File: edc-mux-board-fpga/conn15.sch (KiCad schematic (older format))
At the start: 0 parts

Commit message: copied conn0 sheet to rest of connectors
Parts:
- added C? (x2): 2.2uF X7R, symbol Device:C_Small
- added C? (x6): 1uF, symbol Device:C_Small
- added C? (x8): 100nF, symbol Device:C_Small
- added C? (x2): 33pF, symbol Device:C_Small
- added C? (x2): 10uF, symbol Device:C_Small
- added FB?: 220Ω/2A, Resistor_SMD:R_0603_1608Metric, symbol Device:Ferrite_Bead_Small
- added J?: Device 15, Connector_PinHeader_2.54mm:PinHeader_1x12_P2.54mm_Vertical, symbol Connector_Generic:Conn_01x12
- added R? (x2): 750Ω, symbol Device:R_Small_US
- added U?: TLV320AIC3206, Package_DFN_QFN:UQFN-40-1EP_5x5mm_P0.4mm_EP3.8x3.8mm_ThermalVias, symbol SW-Texas:TLV320AIC3206
- added U?: MAX4910, Package_DFN_QFN:TQFN-16-1EP_3x3mm_P0.5mm_EP1.23x1.23mm, symbol SW-dallas-semi-maxim:MAX4910
- added U?: P82B96, symbol Interface_Expansion:P82B96
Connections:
- new net: C?.1, C?.2, U?.17 (IN1_L)
- new net: C?.1, C?.2, U?.18 (IN1_R)
- new net: C?.2, U?.19 (IN2_L), U?.20 (IN2_R)
- new net: C?.2, U?.22 (REF)
- new net: C?.2, U?.24 (IN3_L), U?.25 (IN3_R)
- new net: C?.2, U?.26 (LINE_OUT_L)
- new net: C?.2, U?.27 (LINE_OUT_R)
- new net: FB?.1, U?.28 (GND_SENSE), U?.3 (NO2)
- new net: U?.15 (NO1), U?.31 (HPL)
- new net: U?.33 (HPR), U?.7 (NO3)
- new net: C?.2, U?.35 (VNEG)
- new net: C?.1, U?.36 (FLY_N)
- new net: C?.2, U?.38 (FLY_P)
- new net: C?.2, J?.2 (Pin_2)
- new net: C?.2, J?.3 (Pin_3)
- new net: C?.1, U?.1 (NC1)
- new net: C?.1, U?.9 (NC3)
- new net +12V: C?.1, J?.12 (Pin_12), R?.1, R?.1, U?.8 (VCC)
- new net +1V8: C?.2, C?.2, U?.30 (VSYS), U?.40 (DVDD)
- new net +1V8A: C?.2, C?.2, C?.2, U?.29 (AVDD), U?.32 (DRVDD_HP), U?.39 (DVDD_CP)
- new net +3V3: C?.1, C?.2, C?.2, U?.10 (IOVDD), U?.14 (VCC)
- new net AUD_GND: J?.1 (Pin_1), U?.4 (COM2)
- new net BCLK: U?.6 (BCLK)
- new net DIN: U?.8 (DIN)
- new net DOUT: U?.9 (DOUT)
- new net GND: C?.1, C?.1, C?.1, C?.1, C?.1, C?.1, C?.1, C?.1, C?.1, C?.1, C?.1, C?.1, C?.1, C?.2, C?.2, FB?.2, J?.6 (Pin_6), U?.1 (DVSS), U?.11 (IOVSS), U?.16 (SPI_SELECT), U?.17 (PAD), U?.2 (DVSS), U?.21 (AVSS), U?.37 (DVSS_CP), U?.4 (GND), U?.41 (PAD), U?.5 (NC2), U?.6 (GND)
- new net GPI: U?.12 (GPI)
- new net HP_~LINE~_SEL: U?.10 (CB2), U?.2 (CB1), U?.4 (INT2_OUT)
- new net ID_PIN: J?.11 (Pin_11)
- new net INT1_OUT: U?.15 (INT1_OUT)
- new net L_OUT: J?.4 (Pin_4), U?.16 (COM1)
- new net MCLK: U?.5 (MCLK)
- new net R_OUT: J?.5 (Pin_5), U?.8 (COM3)
- new net SCL: U?.13 (SCL), U?.7 (SCL)
- new net SCL_HV: J?.8 (Pin_8), R?.2, U?.5 (TXD-SCL), U?.6 (RXD-SCL)
- new net SDA: U?.1 (SDA), U?.14 (SDA)
- new net SDA_HV: J?.7 (Pin_7), R?.2, U?.2 (RXD-SDA), U?.3 (TXD-SDA)
- new net WCLK: U?.7 (WCLK)
- new net ~RESET: U?.3 (~RESET)
- no-connect marks 0 -> 5
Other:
- note added: "33pF caps per datasheet\nlayout for RF rejection\nPut close to input pin"
- note added: "Due to high input resistance (see datasheet)\nthese caps can be much smaller than normal\nStill use film caps for decoupling"
- note added: "HP_~LINE~_SEL controls whether\nL_OUT and R_OUT are connected\nto line out or HP out terminals on\nCODEC"
- note added: "I2C Address Summary:\nCODEC: 0011000 \nMore than 1 P82B96 cannot be on the same circuit"
- note added: "Power up sequence:\n1: Vsys\n2: IOVdd\n3: DVdd\n4: DVdd_CP\n5: AVdd\n6: DRVdd_HP\nMultiple supplies \ncan come\nup together"
- note added: "use film caps for decoupling"

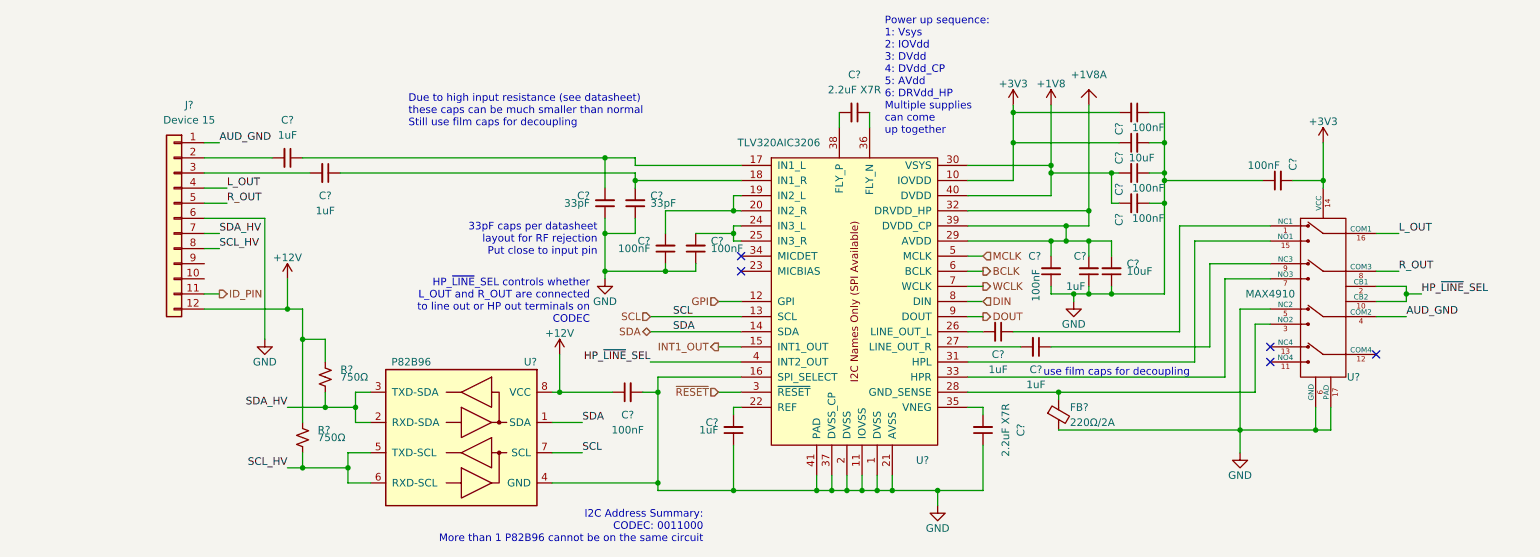
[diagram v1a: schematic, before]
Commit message: Added protection and footprints to all connector subsheets. Added TVS diodes, ferrite beads and made sure all components had footprints assigned
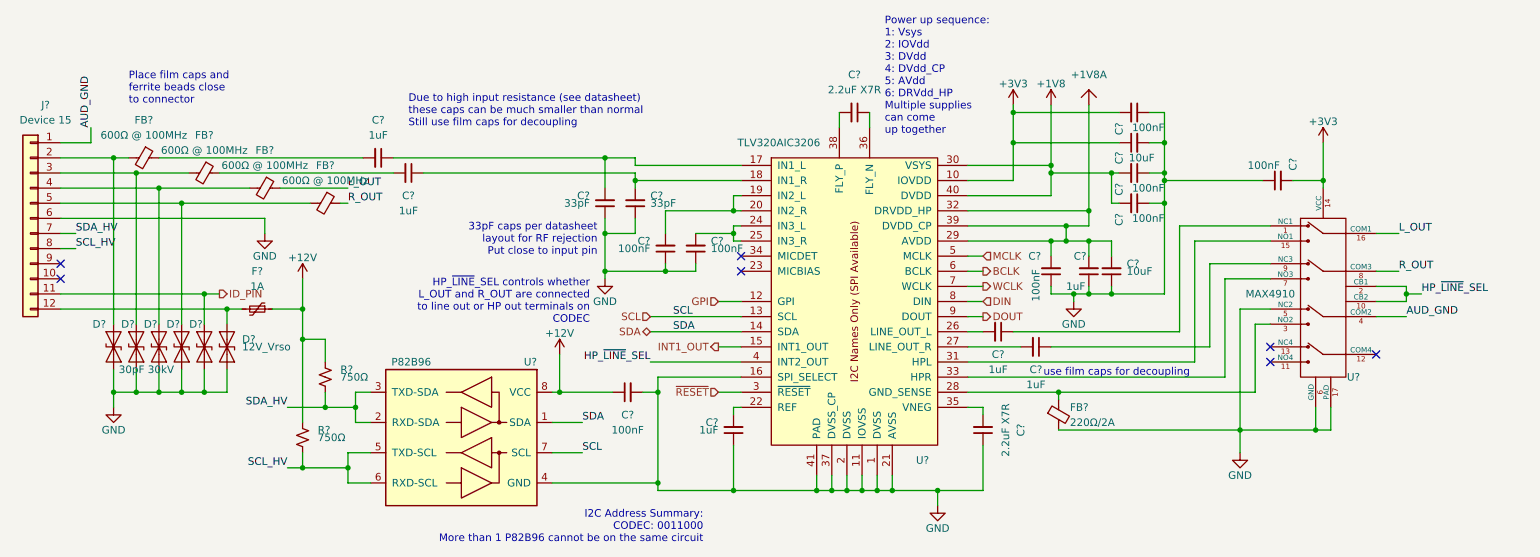
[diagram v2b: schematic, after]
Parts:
- removed C? (x2): 1uF, symbol Device:C_Small
- added C? (x2): 1uF, SW-WIMA:2220_film_cap, symbol Device:C_Small
- added D? (x5): 30pF 30kV, Diode_SMD:D_0402_1005Metric, symbol Device:D_TVS
- added D?: 12V_Vrso, Diode_SMD:D_SMA, symbol Device:D_TVS
- added F?: 1A, Fuse:Fuse_0603_1608Metric, symbol Device:Polyfuse_Small
- added FB? (x4): 600Ω @ 100MHz, Capacitor_SMD:C_0805_2012Metric, symbol Device:Ferrite_Bead_Small
- C? (x14): footprint (none) -> Capacitor_SMD:C_0603_1608Metric
- C? (x2): footprint (none) -> SW-WIMA:2220_film_cap; Manufacturer (none) -> Wima; Manufacturers Part Number (none) -> SMDTC04100QB00KP00
- C? (x2): footprint (none) -> Capacitor_SMD:C_1206_3216Metric; Manufacturer (none) -> Kemet; Manufacturers Part Number (none) -> C1206C106J3RACAUTO; Package ID (none) -> 0603in/1608mm
- R? (x2): footprint (none) -> Resistor_SMD:R_0603_1608Metric
- U?: footprint (none) -> Package_SO:TSSOP-8_3x3mm_P0.65mm
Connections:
- net +12V: now also F?.1; no longer J?.12 (Pin_12)
- net GND: now also D?.2 (A2), D?.2 (A2), D?.2 (A2), D?.2 (A2), D?.2 (A2), D?.2 (A2)
- net ID_PIN: now also D?.1 (A1)
- net L_OUT: now also FB?.1; no longer J?.4 (Pin_4)
- net R_OUT: now also FB?.1; no longer J?.5 (Pin_5)
- net at U?.26 (LINE_OUT_L): now also C?.2
- net at U?.27 (LINE_OUT_R): now also C?.2
- net at C?.2: now also FB?.1; no longer J?.2 (Pin_2)
- net at C?.2: now also FB?.1; no longer J?.3 (Pin_3)
- net at U?.1 (NC1): now also C?.1
- net at U?.9 (NC3): now also C?.1
- new net: D?.1 (A1), F?.2, J?.12 (Pin_12)
- new net: D?.1 (A1), FB?.2, J?.2 (Pin_2)
- new net: D?.1 (A1), FB?.2, J?.3 (Pin_3)
- new net: D?.1 (A1), FB?.2, J?.4 (Pin_4)
- new net: D?.1 (A1), FB?.2, J?.5 (Pin_5)
- no-connect marks 5 -> 7
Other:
- note added: "Place film caps and\nferrite beads close\nto connector"
- moved on the sheet: C?, J?

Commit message: changed footprint for device connector header
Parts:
- J?: footprint Connector_PinHeader_2.54mm:PinHeader_1x12_P2.54mm_Vertical -> Connector_PinHeader_1.27mm:PinHeader_2x06_P1.27mm_Vertical
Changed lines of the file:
@@
 F 0 "J?" H 600 4150 50  0000 C CNN
 F 1 "Device 15" H 600 4050 50  0000 C CNN
-F 2 "Connector_PinHeader_2.54mm:PinHeader_1x12_P2.54mm_Vertical" H 700 3400 50  0001 C CNN
+F 2 "Connector_PinHeader_1.27mm:PinHeader_2x06_P1.27mm_Vertical" H 700 3400 50  0001 C CNN
 F 3 "~" H 700 3400 50  0001 C CNN
 	1    700  3400

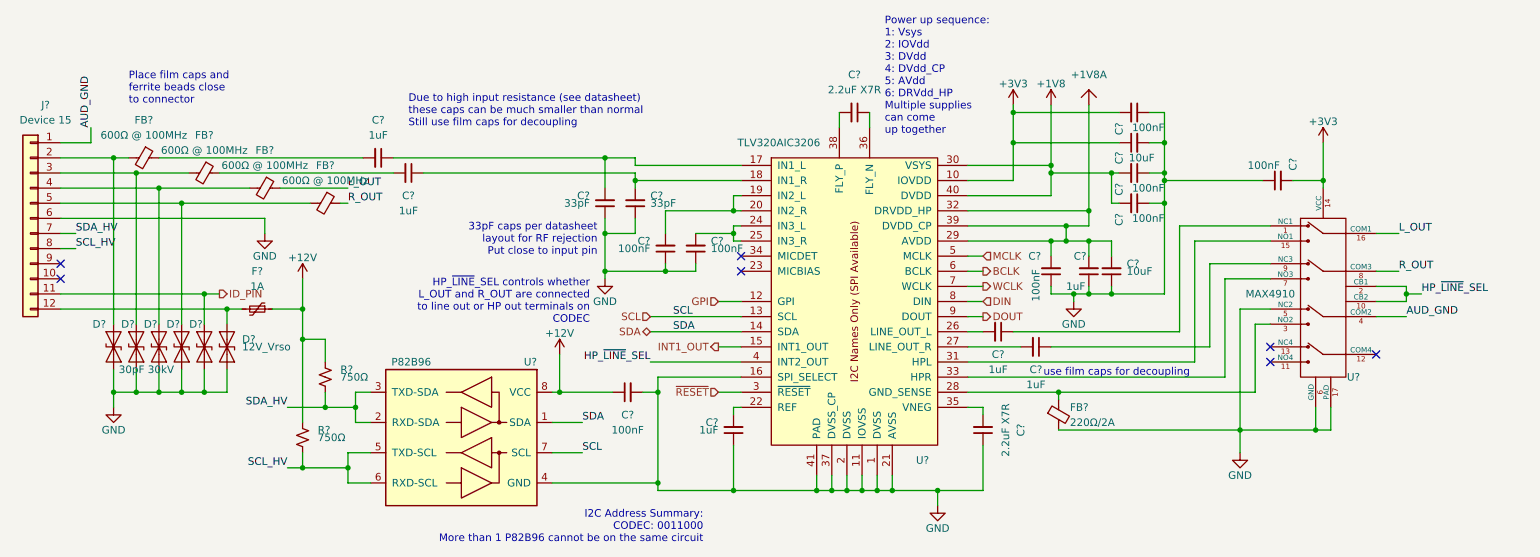
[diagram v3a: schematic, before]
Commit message: annotated board
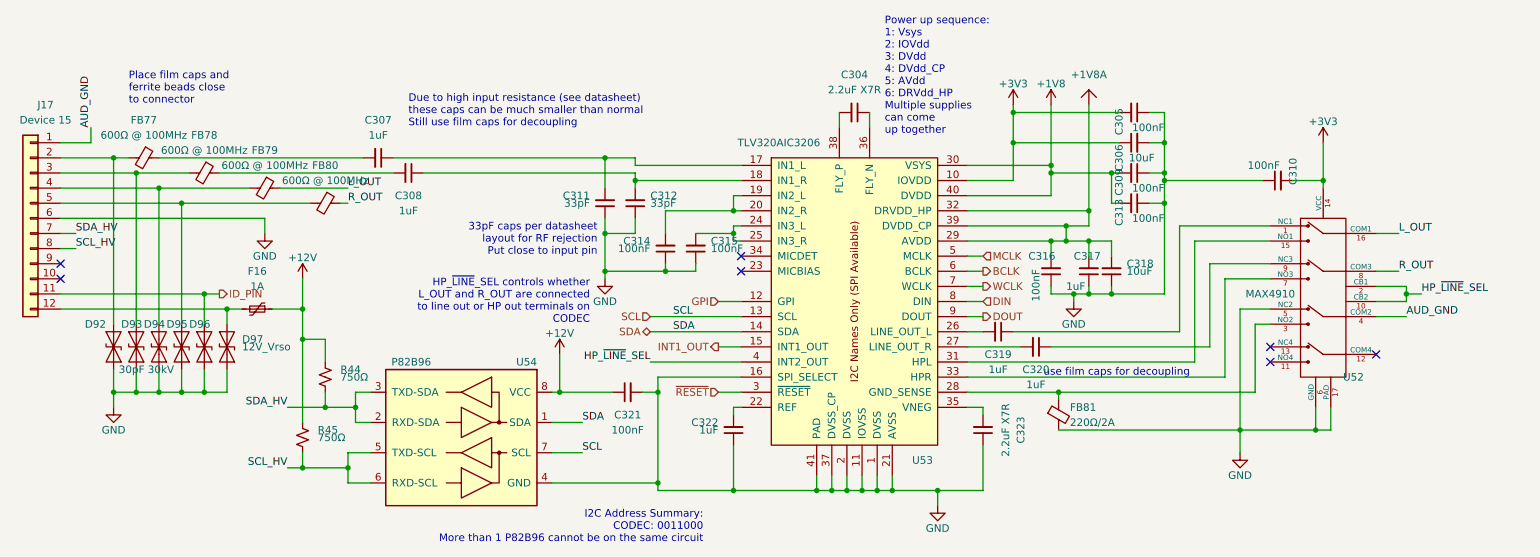
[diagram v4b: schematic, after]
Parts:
- removed C? (x4): 1uF, SW-WIMA:2220_film_cap, symbol Device:C_Small
- removed C? (x2): 2.2uF X7R, Capacitor_SMD:C_0603_1608Metric, symbol Device:C_Small
- removed C?: 1uF, Capacitor_SMD:C_0603_1608Metric, symbol Device:C_Small
- removed C? (x6): 100nF, Capacitor_SMD:C_0603_1608Metric, symbol Device:C_Small
- removed C? (x2): 33pF, Capacitor_SMD:C_0603_1608Metric, symbol Device:C_Small
- removed C? (x2): 10uF, Capacitor_SMD:C_1206_3216Metric, symbol Device:C_Small
- removed D? (x5): 30pF 30kV, Diode_SMD:D_0402_1005Metric, symbol Device:D_TVS
- removed D?: 12V_Vrso, Diode_SMD:D_SMA, symbol Device:D_TVS
- removed F?: 1A, Fuse:Fuse_0603_1608Metric, symbol Device:Polyfuse_Small
- removed FB? (x4): 600Ω @ 100MHz, Capacitor_SMD:C_0805_2012Metric, symbol Device:Ferrite_Bead_Small
- removed FB?: 220Ω/2A, Resistor_SMD:R_0603_1608Metric, symbol Device:Ferrite_Bead_Small
- removed J?: Device 15, Connector_PinHeader_1.27mm:PinHeader_2x06_P1.27mm_Vertical, symbol Connector_Generic:Conn_01x12
- removed R? (x2): 750Ω, Resistor_SMD:R_0603_1608Metric, symbol Device:R_Small_US
- removed U?: TLV320AIC3206, Package_DFN_QFN:UQFN-40-1EP_5x5mm_P0.4mm_EP3.8x3.8mm_ThermalVias, symbol SW-Texas:TLV320AIC3206
- removed U?: P82B96, Package_SO:TSSOP-8_3x3mm_P0.65mm, symbol Interface_Expansion:P82B96
- added C304, C323: 2.2uF X7R, Capacitor_SMD:C_0603_1608Metric, symbol Device:C_Small
- added C305, C313, C314, C315, C316, C321: 100nF, Capacitor_SMD:C_0603_1608Metric, symbol Device:C_Small
- added C306, C318: 10uF, Capacitor_SMD:C_1206_3216Metric, symbol Device:C_Small
- added C307, C308, C319, C320: 1uF, SW-WIMA:2220_film_cap, symbol Device:C_Small
- added C311, C312: 33pF, Capacitor_SMD:C_0603_1608Metric, symbol Device:C_Small
- added C322: 1uF, Capacitor_SMD:C_0603_1608Metric, symbol Device:C_Small
- added D92, D93, D94, D95, D96: 30pF 30kV, Diode_SMD:D_0402_1005Metric, symbol Device:D_TVS
- added D97: 12V_Vrso, Diode_SMD:D_SMA, symbol Device:D_TVS
- added F16: 1A, Fuse:Fuse_0603_1608Metric, symbol Device:Polyfuse_Small
- added FB77, FB78, FB79, FB80: 600Ω @ 100MHz, Capacitor_SMD:C_0805_2012Metric, symbol Device:Ferrite_Bead_Small
- added FB81: 220Ω/2A, Resistor_SMD:R_0603_1608Metric, symbol Device:Ferrite_Bead_Small
- added J17: Device 15, Connector_PinHeader_1.27mm:PinHeader_2x06_P1.27mm_Vertical, symbol Connector_Generic:Conn_01x12
- added R44, R45: 750Ω, Resistor_SMD:R_0603_1608Metric, symbol Device:R_Small_US
- added U53: TLV320AIC3206, Package_DFN_QFN:UQFN-40-1EP_5x5mm_P0.4mm_EP3.8x3.8mm_ThermalVias, symbol SW-Texas:TLV320AIC3206
- added U54: P82B96, Package_SO:TSSOP-8_3x3mm_P0.65mm, symbol Interface_Expansion:P82B96
- gave numbers to parts that had none: 4
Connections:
- net +12V: now also C321.1, F16.1, R44.1, R45.1, U54.8 (VCC)
- net +1V8: now also C313.2, U53.30 (VSYS), U53.40 (DVDD)
- net +1V8A: now also C316.2, C318.2, U53.29 (AVDD), U53.32 (DRVDD_HP), U53.39 (DVDD_CP)
- net +3V3: now also C305.2, C306.1, U53.10 (IOVDD)
- net AUD_GND: now also J17.1 (Pin_1)
- net BCLK: now also U53.6 (BCLK)
- net DIN: now also U53.8 (DIN)
- net DOUT: now also U53.9 (DOUT)
- net GND: now also C305.1, C306.2, C311.1, C312.1, C313.1, C314.1, C315.1, C316.1, C318.1, C321.2, C322.1, C323.1, D92.2 (A2), D93.2 (A2), D94.2 (A2), D95.2 (A2), D96.2 (A2), D97.2 (A2), FB81.2, J17.6 (Pin_6), U53.1 (DVSS), U53.11 (IOVSS), U53.16 (SPI_SELECT), U53.2 (DVSS), U53.21 (AVSS), U53.37 (DVSS_CP), U53.41 (PAD), U54.4 (GND)
- net GPI: now also U53.12 (GPI)
- net HP_~LINE~_SEL: now also U53.4 (INT2_OUT)
- net ID_PIN: now also D96.1 (A1), J17.11 (Pin_11)
- net INT1_OUT: now also U53.15 (INT1_OUT)
- net L_OUT: now also FB79.1
- net MCLK: now also U53.5 (MCLK)
- net R_OUT: now also FB80.1
- net SCL: now also U53.13 (SCL), U54.7 (SCL)
- net SCL_HV: now also J17.8 (Pin_8), R45.2, U54.5 (TXD-SCL), U54.6 (RXD-SCL)
- net SDA: now also U53.14 (SDA), U54.1 (SDA)
- net SDA_HV: now also J17.7 (Pin_7), R44.2, U54.2 (RXD-SDA), U54.3 (TXD-SDA)
- net WCLK: now also U53.7 (WCLK)
- net ~RESET: now also U53.3 (~RESET)
- net at U52.1 (NC1): now also C319.1
- net at U52.9 (NC3): now also C320.1
- net at U52.3 (NO2): now also FB81.1, U53.28 (GND_SENSE)
- net at U52.15 (NO1): now also U53.31 (HPL)
- net at U52.7 (NO3): now also U53.33 (HPR)
- new net: D97.1 (A1), F16.2, J17.12 (Pin_12)
- new net: C307.2, FB77.1
- new net: D92.1 (A1), FB77.2, J17.2 (Pin_2)
- new net: C308.2, FB78.1
- new net: D93.1 (A1), FB78.2, J17.3 (Pin_3)
- new net: D94.1 (A1), FB79.2, J17.4 (Pin_4)
- new net: D95.1 (A1), FB80.2, J17.5 (Pin_5)
- new net: C319.2, U53.26 (LINE_OUT_L)
- new net: C320.2, U53.27 (LINE_OUT_R)
- new net: C307.1, C311.2, U53.17 (IN1_L)
- new net: C308.1, C312.2, U53.18 (IN1_R)
- new net: C314.2, U53.19 (IN2_L), U53.20 (IN2_R)
- new net: C322.2, U53.22 (REF)
- new net: C315.2, U53.24 (IN3_L), U53.25 (IN3_R)
- new net: C323.2, U53.35 (VNEG)
- new net: C304.1, U53.36 (FLY_N)
- new net: C304.2, U53.38 (FLY_P)
